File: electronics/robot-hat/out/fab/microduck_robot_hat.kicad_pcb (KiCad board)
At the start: 2 copper layers, 65 x 30 mm, 28 parts, among them J1 40-pin GPIO, J2 VBAT in (B2B-XH-A), J3 DXL bus (B3B-EH-A), J5 Stemma J5 (SM04B-SRSS-TB), J6 speaker (B2B-PH-K-S), J7 mic (B3B-PH-K-S), U1 TLV320AIC3104, U2 Pololu D30V30F5, U3 BMI088 (dormant), U4 74LVC1G125

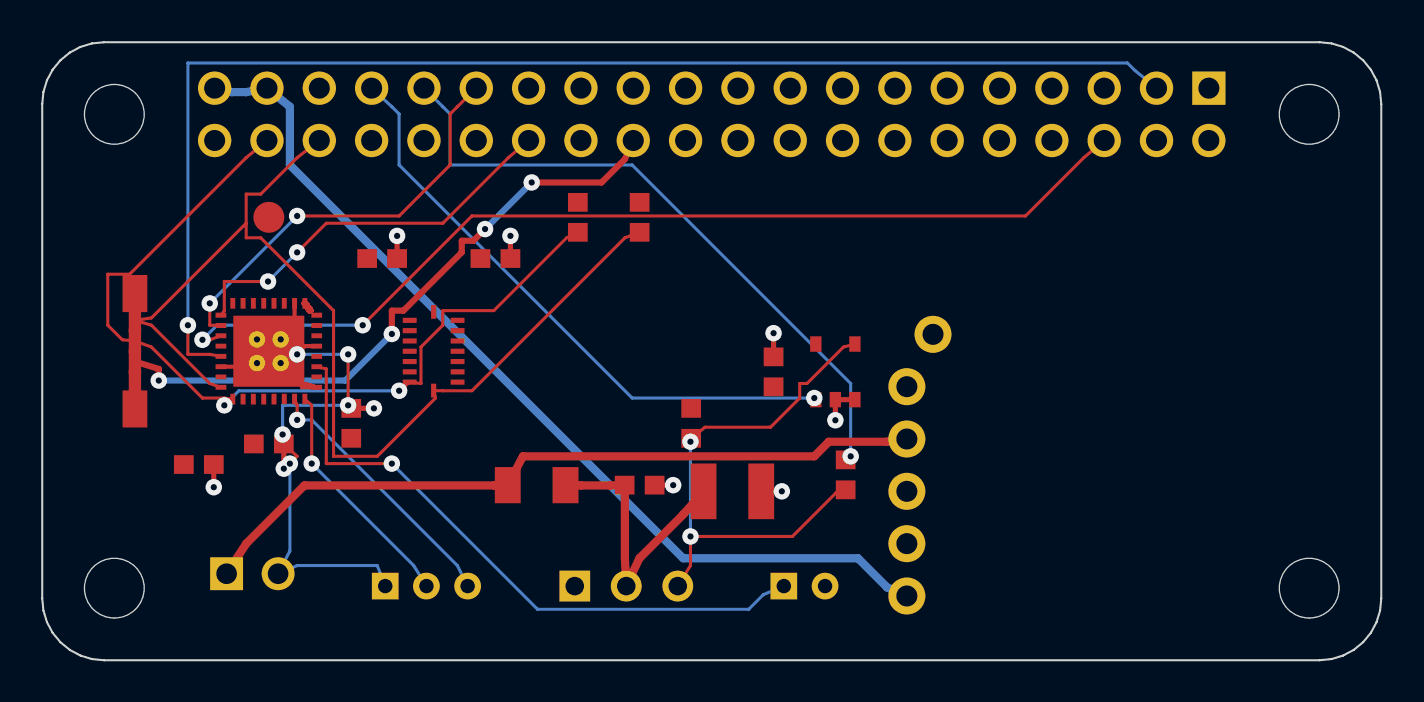
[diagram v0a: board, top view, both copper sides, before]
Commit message: SIM-CAPABILITY.md — our stack vs SolidWorks, measured; MuJoCo runs Pollen's policies 77x real time; robotd-in-the-loop (Dynamixel register model backed by mj_step) is the bounded missing piece; Isaac Sim needs RTX we lack
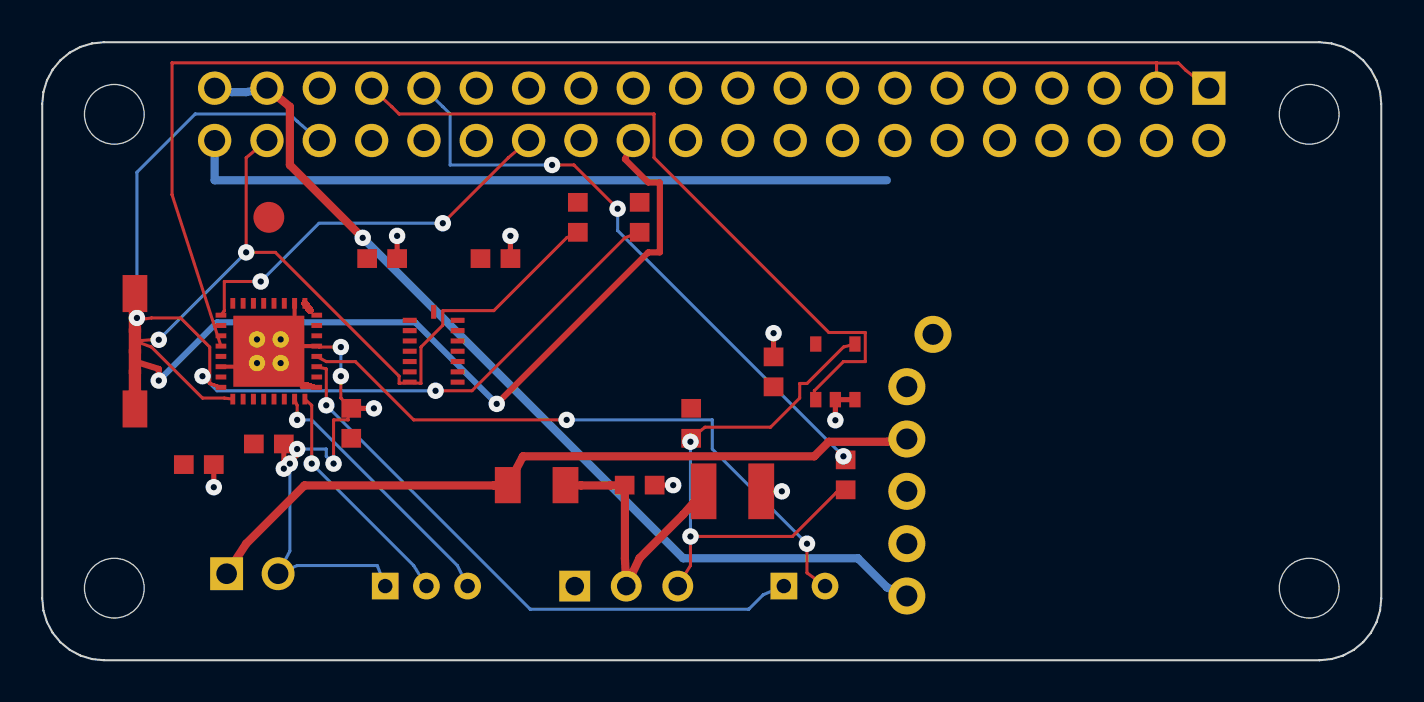
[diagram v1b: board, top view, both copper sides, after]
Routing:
- net GND: track 193.6 -> 506.2 mm
- net HAT_3V3: track 79.2 -> 383.1 mm
- net i2s3/DIN: track 0.00 -> 66.1 mm
- net i2s3/DOUT: track 63.2 -> 0.00 mm, vias 1 -> 0
- net i2s3/WCLK: track 48.7 -> 0.00 mm, vias 2 -> 0
- net SPK_N: track 0.00 -> 30.9 mm, vias 0 -> 2
- net i2s3/BCLK: track 20.3 -> 0.00 mm, vias 2 -> 0
- net J5_3V3: track 30.8 -> 38.5 mm, vias 4 -> 2
- net uart2/TX: track 29.3 -> 35.0 mm, vias 1 -> 0
- net uart2/RX: track 31.9 -> 30.0 mm, vias 1 -> 3
- net SPK_P: track 30.6 -> 28.9 mm
- net i2c3/SCL: track 51.8 -> 50.2 mm, vias 0 -> 3
- net i2c3/SDA: track 42.8 -> 42.3 mm
- net V5_HAT: vias 0 -> 1

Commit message: lane D: both boards re-routed with the measured fixes; Robot HAT 10 FAIL -> 8
Robot HAT, 44 pass / 8 fail / 3 cannot determine: the three 0.000 mm clearance
rows the i2s3/DIN spine used to produce are GONE - it now leaves J1 pad 40,
which is the pin that actually carries that net (Radxa brief RAD-DOC-0084: pin
40 GPIO3_A5 I2S3_SDO_M0) - and i2s3/BCLK now routes. What is left is one
hole-to-hole via/via and seven open nets. Widening VBAT / SERVO_V / V5_HAT
from 0.400 to 0.800 mm bought copper capacity (1.231 A -> 2.034 A at dT 10)
and cost two routes.

imu_to_dxl, 36 pass / 3 fail / 3 cannot determine, 40/53 routed: every
remaining failure is 'unrouted' - no clearance, no hole-to-hole, no courtyard.
Silk fixed after reading the plot back: two legends were printed on the same
line at y = 8.000 and overlapped; the long one moved to B.Silk.

Both boards' out/fab/ now carries ORDER-NOTES.txt inside the zip. The Robot
HAT's own silk still runs off the right edge - recorded OPEN in section 1.1
rather than fixed, because that board needs a re-route for U2's height anyway
and a 40-minute routing run to move a legend is the wrong order to work in.
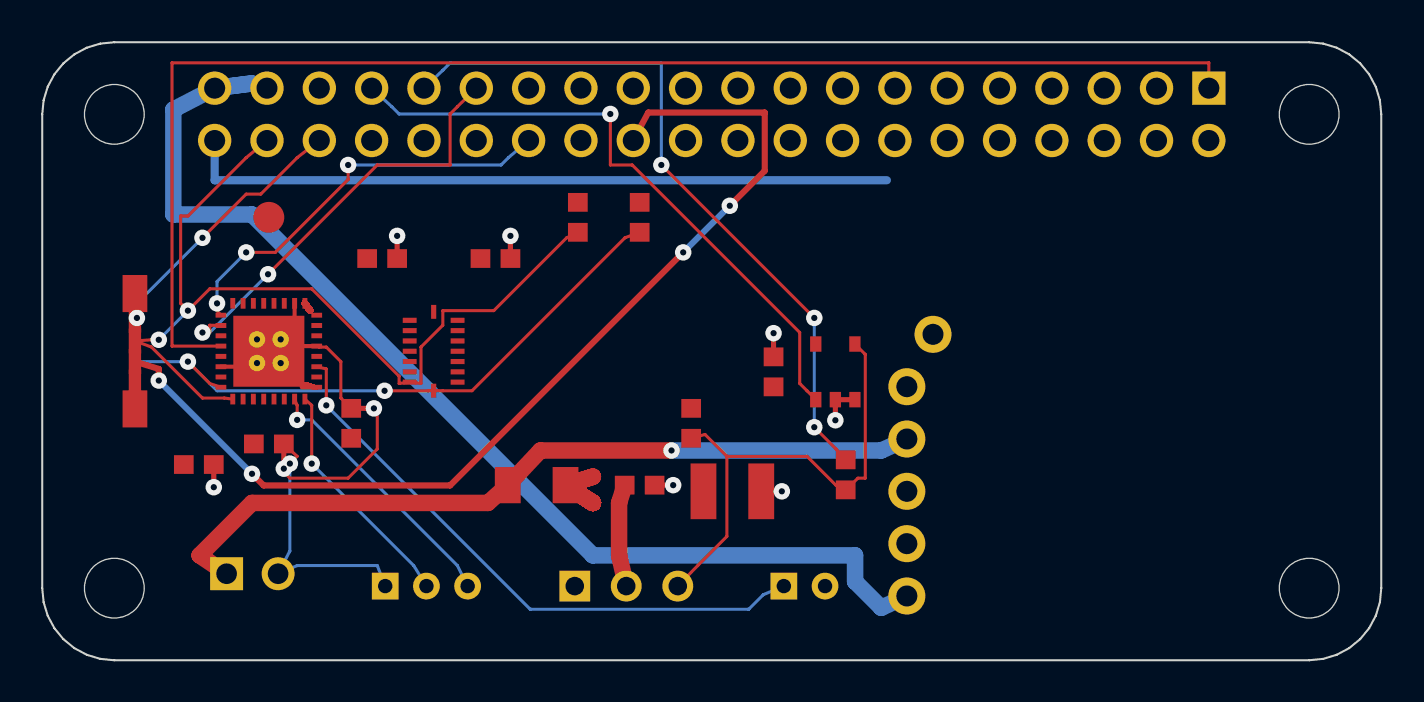
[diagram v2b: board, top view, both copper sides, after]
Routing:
- net SERVO_V: track 13.8 -> 67.5 mm
- net SPK_N: track 30.9 -> 0.00 mm, vias 2 -> 0
- net i2s3/BCLK: track 0.00 -> 20.9 mm, vias 0 -> 2
- net J5_3V3: track 38.5 -> 49.7 mm, vias 2 -> 4
- net V5_HAT: track 45.4 -> 55.4 mm, vias 1 -> 0
- net i2c3/SCL: track 50.2 -> 45.2 mm, vias 3 -> 4
- net uart2/RX: track 30.0 -> 35.0 mm
- net uart2/TX: track 35.0 -> 30.7 mm, vias 0 -> 1
- net i2c3/SDA: track 42.3 -> 45.3 mm
- net dxl/DATA: track 26.0 -> 23.8 mm, vias 2 -> 0
- net VBAT: track 36.1 -> 38.2 mm, vias 0 -> 1
- net i2s3/DIN: track 66.1 -> 67.7 mm
- net i2s3/MCLK: track 19.3 -> 20.0 mm, vias 2 -> 3
- net GND: track 506.2 -> 506.9 mm, vias 14 -> 10
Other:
- outline, holes or cut-outs redrawn
